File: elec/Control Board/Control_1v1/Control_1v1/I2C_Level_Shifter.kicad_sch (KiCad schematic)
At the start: 21 parts, among them J201 0.100_2Pin, J202 Conn_01x04, Q201 BSS138, Q202 BSS138

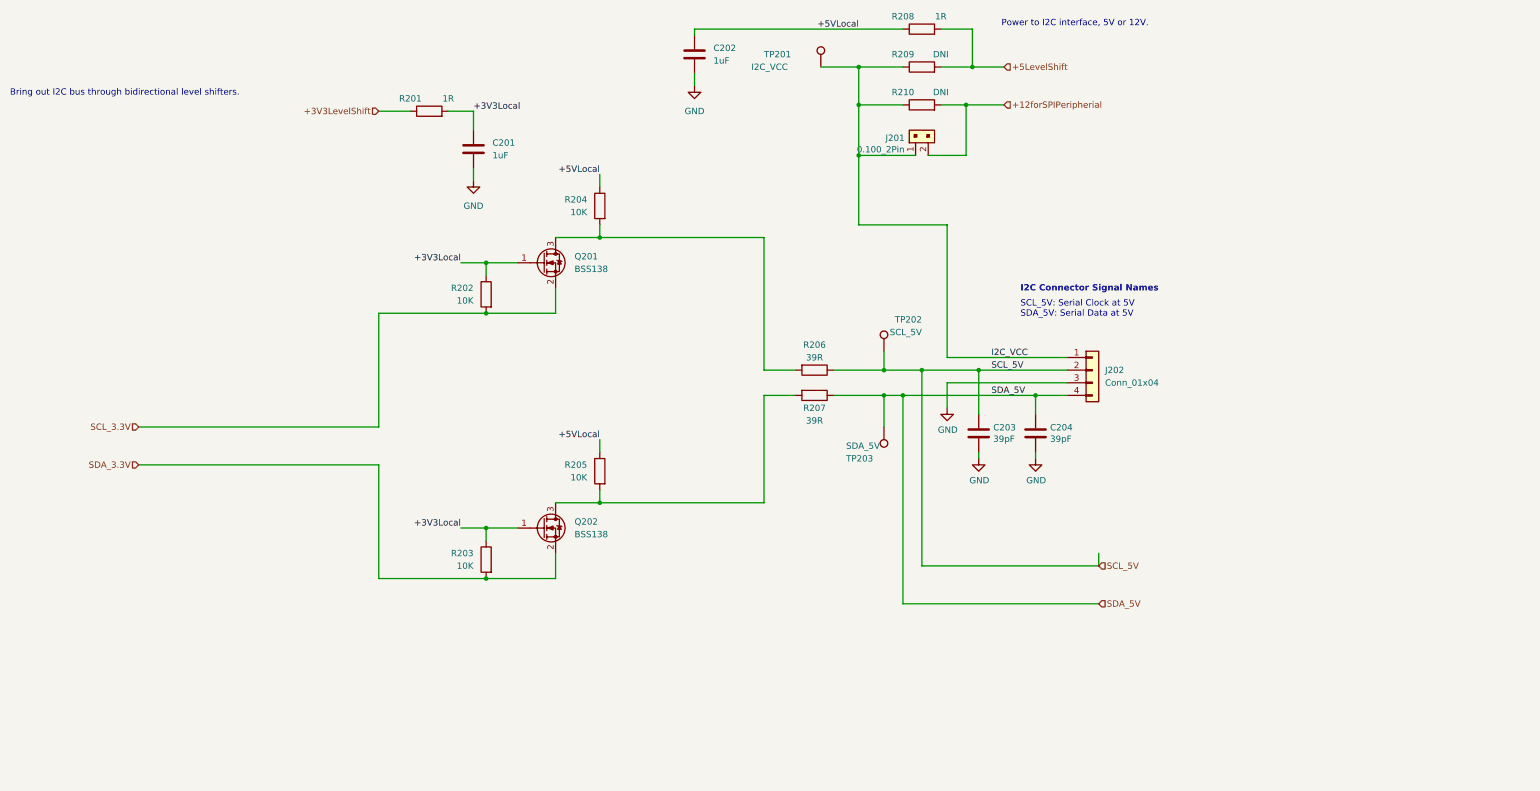
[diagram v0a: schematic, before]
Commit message: Add sheet with title block.
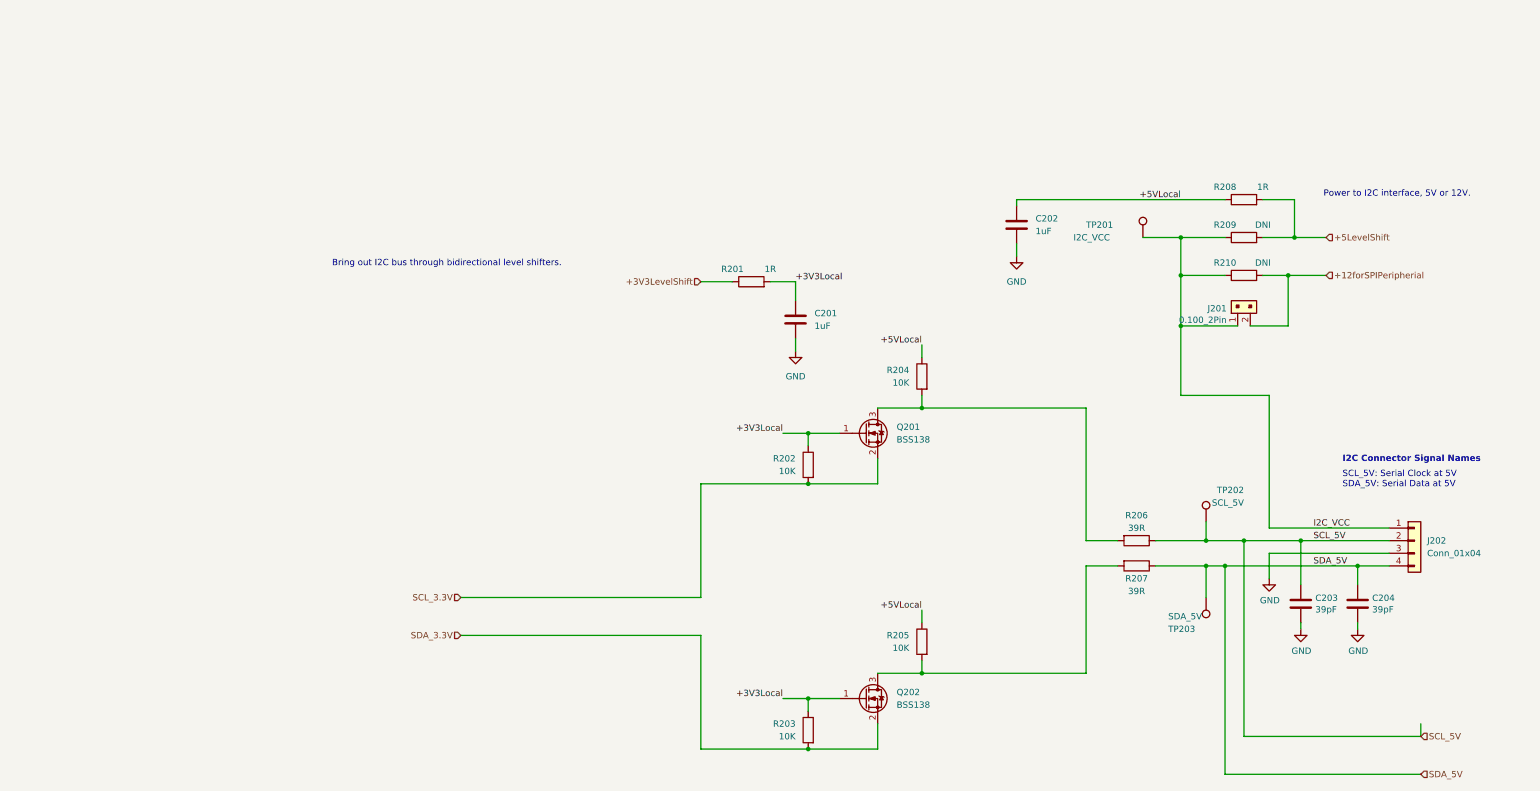
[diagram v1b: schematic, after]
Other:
- company: (none) -> Public Invention
- title: (none) -> Control Interconnect Board
- moved on the sheet: C201, C202, C203, C204, J201, J202, Q201, Q202, R201, R202, R203, R204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

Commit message: Fix J10 backwards.
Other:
- title: Control Interconnect Board -> Control Interconnect Board OEDCS
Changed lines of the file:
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@@
   (paper "USLedger")
   (title_block
-    (title "Control Interconnect Board")
+    (title "Control Interconnect Board OEDCS")
     (date "2023-10-10")
     (rev "Rev 1.1")
     (company "Public Invention")
-    (comment 1 "Contributor: Lawrence Kinceloe")
+    (comment 1 "GNU Affero General Public License v3.0")
+    (comment 2 "Contributor: Lawrence Kinceloe")
+    (comment 3 "Drawn By: (Forrest) Lee Erickson")
   )
   (junction (at 270.51 129.54) (diameter 0) (color 0 0 0 0)

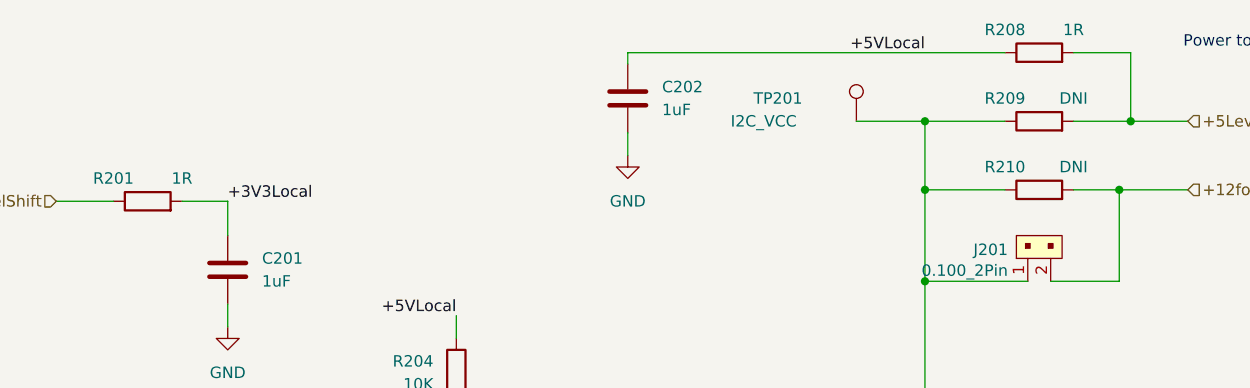
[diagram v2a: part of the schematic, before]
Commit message: Add power shutdown button. Add thermocouple ground screw terminals. Isolate SCL from SDA traces. Make first cut BOM.
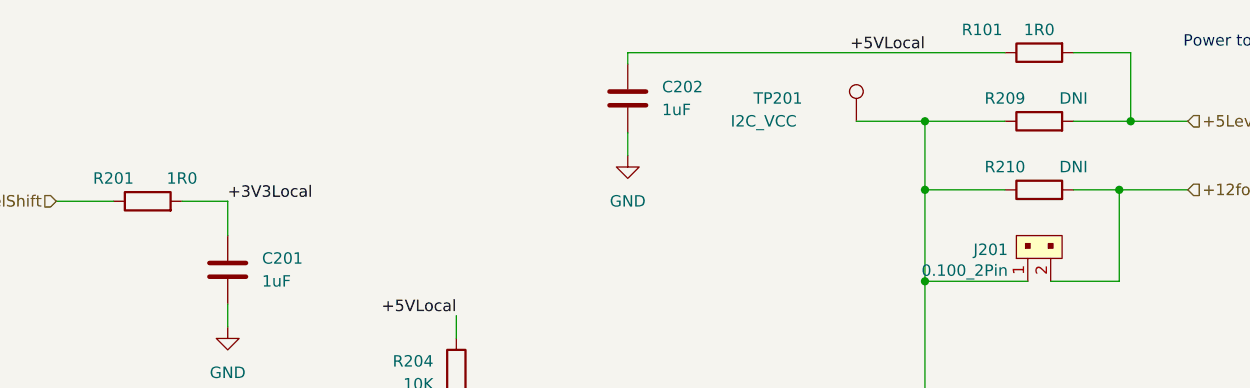
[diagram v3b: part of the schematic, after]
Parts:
- removed R208: 1R, Resistor_SMD:R_0603_1608Metric_Pad0.98x0.95mm_HandSolder, symbol Device:R
- added R101: 1R0, Resistor_SMD:R_0603_1608Metric_Pad0.98x0.95mm_HandSolder, symbol Device:R
- R201: value 1R -> 1R0; Distributor 1 NA -> JLCPCB; Distributor 1 PN NA -> C269434; MPN (none) -> RMC060315%N; Manufacturer (none) -> TyoHM
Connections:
- net +5LevelShift: now also R101.2
- net +5VLocal: now also R101.1
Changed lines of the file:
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@@
       (effects (font (size 1.27 1.27)))
     )
-    (property "Value" "1R" (at 163.83 74.93 90)
+    (property "Value" "1R0" (at 163.83 74.93 90)
       (effects (font (size 1.27 1.27)))
     )
@@
       (effects (font (size 1.27 1.27)) hide)
     )
-    (property "Distributor 1" "NA" (at 160.02 77.47 0)
-      (effects (font (size 1.27 1.27)) hide)
-    )
-    (property "Distributor 1 PN" "NA" (at 160.02 77.47 0)
+    (property "Distributor 1" "JLCPCB" (at 160.02 77.47 0)
+      (effects (font (size 1.27 1.27)) hide)
+    )
+    (property "Distributor 1 PN" "C269434" (at 160.02 77.47 0)
       (effects (font (size 1.27 1.27)) hide)
     )
@@
       (effects (font (size 1.27 1.27)) hide)
     )
-    (property "Description" "Do Not Insert" (at 160.02 77.47 0)
+    (property "Description" "0.1W ±5% 1Ω 0603 Chip Resistor - Surface Mount ROHS" (at 160.02 77.47 0)
+      (effects (font (size 1.27 1.27)) hide)
+    )
+    (property "MPN" "RMC060315%N" (at 160.02 77.47 0)
+      (effects (font (size 1.27 1.27)) hide)
+    )
+    (property "Manufacturer" "TyoHM" (at 160.02 77.47 0)
       (effects (font (size 1.27 1.27)) hide)
     )
@@
     )
   )
-  (symbol (lib_id "Device:R") (at 259.08 60.96 90) (unit 1)
+  (symbol (lib_id "Device:R") (at 259.08 60.96 90) (mirror x) (unit 1)
     (in_bom yes) (on_board yes) (dnp no)
-    (property "Reference" "R208" (at 255.27 58.42 90)
-      (effects (font (size 1.27 1.27)))
-    )
-    (property "Value" "1R" (at 262.89 58.42 90)
-      (effects (font (size 1.27 1.27)))
-    )
-    (property "Footprint" "Resistor_SMD:R_0603_1608Metric_Pad0.98x0.95mm_HandSolder" (at 259.08 62.738 90)
+    (property "Reference" "R101" (at 252.73 58.42 90)
+      (effects (font (size 1.27 1.27)))
+    )
+    (property "Value" "1R0" (at 259.08 58.42 90)
+      (effects (font (size 1.27 1.27)))
+    )
+    (property "Footprint" "Resistor_SMD:R_0603_1608Metric_Pad0.98x0.95mm_HandSolder" (at 259.08 59.182 90)
       (effects (font (size 1.27 1.27)) hide)
     )
@@
       (effects (font (size 1.27 1.27)) hide)
     )
+    (property "Distributor 1" "JLCPCB" (at 259.08 60.96 90)
+      (effects (font (size 1.27 1.27)) hide)
+    )
+    (property "Distributor 1 PN" "C269434" (at 259.08 60.96 90)
+      (effects (font (size 1.27 1.27)) hide)
+    )
+    (property "Manufacturer" "TyoHM" (at 259.08 60.96 90)
+      (effects (font (size 1.27 1.27)) hide)
+    )
+    (property "MPN" "RMC060315%N" (at 259.08 60.96 90)
+      (effects (font (size 1.27 1.27)) hide)
+    )
+    (property "Description" "0.1W ±5% 1Ω 0603 Chip Resistor - Surface Mount ROHS" (at 259.08 60.96 0)
+      (effects (font (size 1.27 1.27)) hide)
+    )
     (property "AssemblyType" "SMT" (at 259.08 60.96 0)
       (effects (font (size 1.27 1.27)) hide)
     )
-    (property "Distributor 1" "NA" (at 259.08 60.96 0)
-      (effects (font (size 1.27 1.27)) hide)
-    )
-    (property "Distributor 1 PN" "NA" (at 259.08 60.96 0)
-      (effects (font (size 1.27 1.27)) hide)
-    )
     (property "Cost" "0.0015" (at 259.08 60.96 0)
       (effects (font (size 1.27 1.27)) hide)
@@
       (effects (font (size 1.27 1.27)) hide)
     )
-    (property "Description" "Do Not Insert" (at 259.08 60.96 0)
-      (effects (font (size 1.27 1.27)) hide)
-    )
-    (pin "1")
-    (pin "2")
-    (instances
-      (project "fan_I2C"
-        (path "/27e09928-2db5-4ece-9e90-f2a9a0b91b8d/09141fd0-c295-4cc6-88a0-924ace0abc49"
-          (reference "R208") (unit 1)
-        )
-      )
-      (project "Control_1v1"
+    (pin "1")
+    (pin "2")
+    (instances
+      (project "GeneralPurposeAlarmDevicePCB"
+        (path "/412a327d-1ee3-473e-bc00-1545004b7edf"
+          (reference "R101") (unit 1)
+        )
+      )
+      (project "Control_1v1"
+        (path "/c68c9deb-8d4d-42f0-adf8-4d3022f4ee59/0cb2f0dc-fe38-451d-b752-5d12a98f8d03"
+          (reference "R9") (unit 1)
+        )
+        (path "/c68c9deb-8d4d-42f0-adf8-4d3022f4ee59"
+          (reference "R8") (unit 1)
+        )
+        (path "/c68c9deb-8d4d-42f0-adf8-4d3022f4ee59/3ff32a52-b1ed-4756-8661-90a95f721605"
+          (reference "R7") (unit 1)
+        )
+        (path "/c68c9deb-8d4d-42f0-adf8-4d3022f4ee59/3daed20d-8623-449a-af6f-871db7628ab2"
+          (reference "R20") (unit 1)
+        )
         (path "/c68c9deb-8d4d-42f0-adf8-4d3022f4ee59/905a527a-e45b-4998-adf0-069f9c917f28"
           (reference "R73") (unit 1)
